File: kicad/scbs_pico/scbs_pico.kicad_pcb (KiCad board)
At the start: 2 copper layers, 60 x 60 mm, 64 parts, among them J1 Conn_01x06_Male, J2 Conn_ARM_JTAG_SWD_10, Q1 2N2907, Q2 2N7002, Q3 MMBT3904, Q4 MMBT3904, U1 TLV9062xD, U2 PC817, U3 Pico

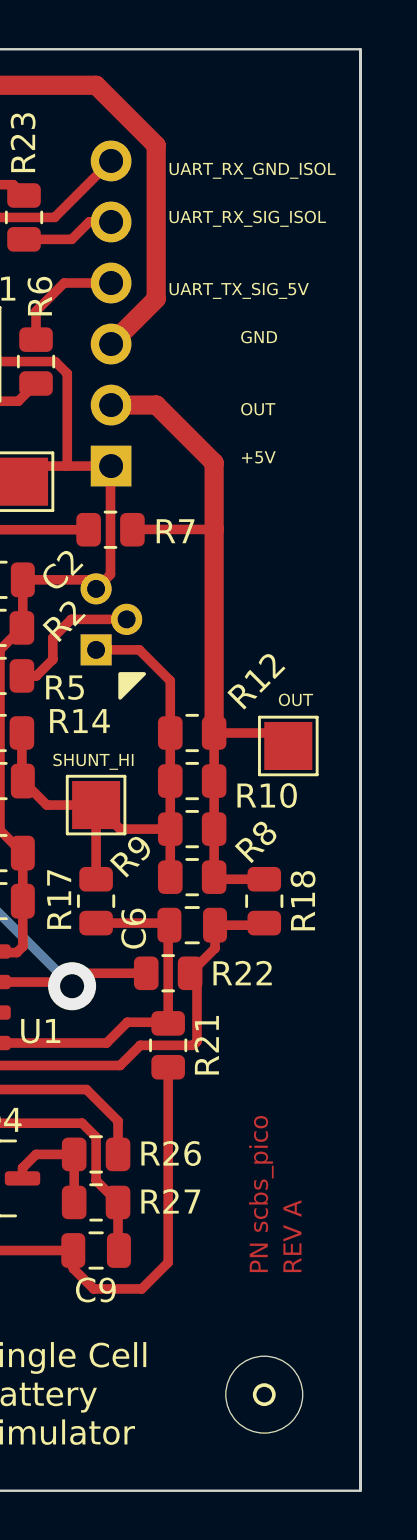
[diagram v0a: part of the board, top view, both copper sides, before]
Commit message: Add SCBS array PCBA Rev A
* Update design notebook.
* Export some stuff for SCBS Pico.
* Create SCBS Array motherboard.
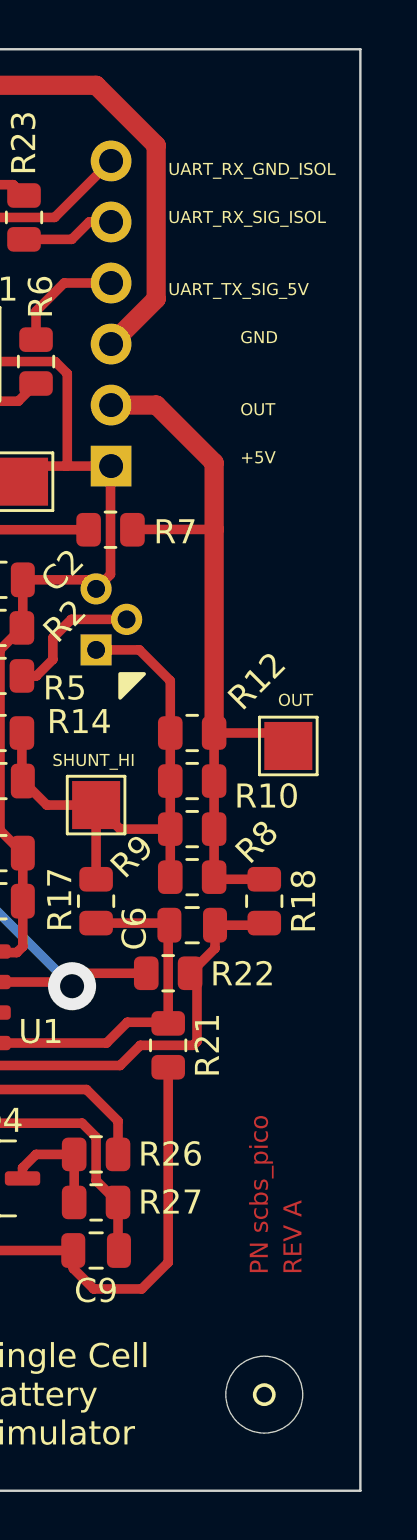
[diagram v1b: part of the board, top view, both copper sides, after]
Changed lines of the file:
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@@
   (gr_line (start 85 80) (end 85 20) (layer "Edge.Cuts") (width 0.1))
   (gr_line (start 25 20) (end 85 20) (layer "Edge.Cuts") (width 0.1))
-  (gr_line (start 85 20) (end 85 80) (layer "Edge.Cuts") (width 0.1))
   (gr_text "CMD_PWM" (at 68.1 72.9) (layer "F.SilkS")
     (effects (font (size 0.5 0.5) (thickness 0.125)))
@@
     (effects (font (size 0.5 0.5) (thickness 0.125)))
   )
+  (dimension (type aligned) (layer "Dwgs.User")
+    (pts (xy 85 80) (xy 85 20))
+    (height 6)
+    (gr_text "60.0000 mm" (at 89.85 50 90) (layer "Dwgs.User")
+      (effects (font (size 1 1) (thickness 0.15)))
+    )
+    (format (units 3) (units_format 1) (precision 4))
+    (style (thickness 0.15) (arrow_length 1.27) (text_position_mode 0) (extension_height 0.58642) (extension_offset 0.5) keep_text_aligned)
+  )
+  (dimension (type aligned) (layer "Dwgs.User")
+    (pts (xy 25 20) (xy 85 20))
+    (height -3)
+    (gr_text "60.0000 mm" (at 55 15.85) (layer "Dwgs.User")
+      (effects (font (size 1 1) (thickness 0.15)))
+    )
+    (format (units 3) (units_format 1) (precision 4))
+    (style (thickness 0.15) (arrow_length 1.27) (text_position_mode 0) (extension_height 0.58642) (extension_offset 0.5) keep_text_aligned)
+  )
+  (dimension (type aligned) (layer "Dwgs.User")
+    (pts (xy 74.625 37.35) (xy 74.6 20))
+    (height 12.998977)
+    (gr_text "17.3500 mm" (at 88.761463 28.654613 -89.9174413) (layer "Dwgs.User")
+      (effects (font (size 1 1) (thickness 0.15)))
+    )
+    (format (units 3) (units_format 1) (precision 4))
+    (style (thickness 0.15) (arrow_length 1.27) (text_position_mode 0) (extension_height 0.58642) (extension_offset 0.5) keep_text_aligned)
+  )
   (segment (start 63.925 55.475) (end 61.94 57.46) (width 0.25) (layer "F.Cu") (net 1))

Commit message: SCBS Array design, add single cell packets
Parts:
- C1, C7: value 0.1uF -> 1nF
- R1, R20: value 2k -> 2M
- R10, R8, R9: value 4R 1% 0805 -> 3.9R 1% 0805
- R11, R15: value 10k -> 10M
- R12: value 4R 1% 0805 -> 4.3R 1% 0805
- R13: value 0R -> 100R
- R17, R18: value 500k 0.1% -> 510k 1%
- R21, R22: value 8.25M 0.1% -> 8.2M 1%
- R5: value 100R -> 750R
